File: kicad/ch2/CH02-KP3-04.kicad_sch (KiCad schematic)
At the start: 7 parts

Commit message: regular
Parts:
- removed I6: 5, symbol Simulation_SPICE:IDC
- removed R29: 10, symbol Device:R_US
- removed R30: 3, symbol Device:R_US
- removed R31, R32: 6, symbol Device:R_US
- removed R33: 16, symbol Device:R_US
- removed V12: 30, symbol Simulation_SPICE:VDC
- added G1: GSOURCE, symbol Simulation_SPICE:GSOURCE
- added I7: 5m, symbol Simulation_SPICE:IDC
- added R34: 10k, symbol Device:R_US
- added R35: 5k, symbol Device:R_US
- added R36: 20k, symbol Device:R_US
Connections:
- net 0: now also G1.1 (N+), G1.4 (C-), I7.1, R34.2, R35.2, R36.2
- new net: G1.2 (N-), R35.1, R36.1
- new net Vo: G1.3 (C+), I7.2, R34.1

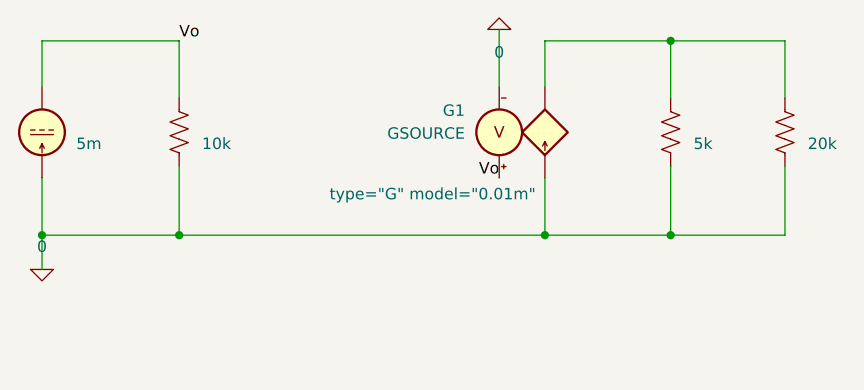
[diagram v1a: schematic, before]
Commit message: fix subsheet sim problem
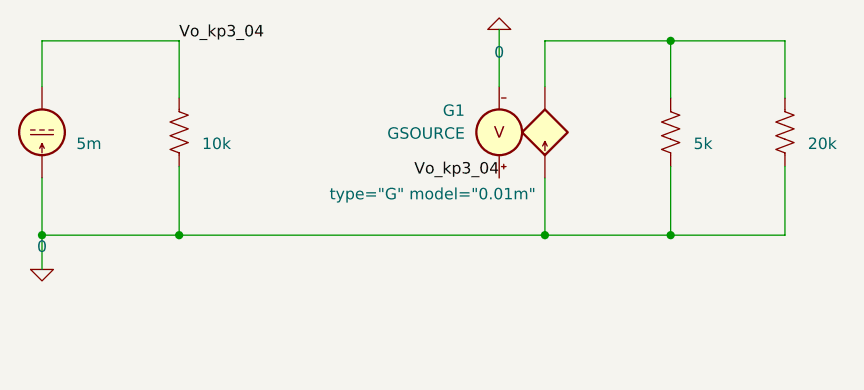
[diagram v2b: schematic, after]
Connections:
- net Vo renamed Vo_kp3_04
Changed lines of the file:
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@@
 		)
 	)
-	(label "Vo"
+	(label "Vo_kp3_04"
 		(at 78.74 67.31 0)
 		(effects
@@
 		)
 	)
-	(label "Vo"
+	(label "Vo_kp3_04"
 		(at 114.3 82.55 180)
 		(effects
